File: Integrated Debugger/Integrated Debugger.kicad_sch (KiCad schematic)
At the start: 26 parts, among them J1 B2B GT-B0353FSV06-08B0201, J2 USB_C (PC <-> Host), U2 USBULC6-2M6

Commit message: feat: finish routing of components
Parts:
- removed D1: GREEN, symbol Picoballoon Passives:LED
- removed R4, R5, R6, R7: 100Ω, Picoballoon Passives:Resistor 0201, symbol Picoballoon Passives:Resistor
- removed TP1: SWDIO, symbol Connector:TestPoint_Small
- removed TP2: SWCLK, symbol Connector:TestPoint_Small
- removed TP3: NRST, symbol Connector:TestPoint_Small
- removed TP4: SWO, symbol Connector:TestPoint_Small
- removed TP5: D-, symbol Connector:TestPoint_Small
- removed TP6: D+, symbol Connector:TestPoint_Small
- added RN1: 100Ω, Picoballoon Passives:Resistor Pack YC248-JR-07100RL, symbol Picoballoon Passives:R_Pack08_Split
- D3, D4, D5: footprint (none) -> Picoballoon Passives:LED 0201
- R10, R8, R9: value 100Ω -> 1.5kΩ
- TP1: renamed from TP7; footprint (none) -> Picoballoon Mechanical & Misc:TestPoint
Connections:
- net MCU/LED0: now also R10.2; no longer D3.1 (K)
- net MCU/LED1: now also R9.2; no longer D4.1 (K)
- net MCU/LED2: now also R8.2; no longer D5.1 (K)
- net Target Frontend/xRST: now also RN1.16 (R1.2)
- net Target Frontend/xRXD: now also RN1.9 (R8.2)
- net Target Frontend/xTCK: now also RN1.13 (R4.2); no longer R10.1
- net Target Frontend/xTDI: now also RN1.15 (R2.2)
- net Target Frontend/xTDO: now also RN1.12 (R5.2); no longer R9.1
- net Target Frontend/xTMS: now also RN1.14 (R3.2)
- net Target Frontend/xTXD: now also RN1.11 (R6.2); no longer R8.1
- net Target/tRST: now also RN1.1 (R1.1)
- net Target/tRXD: now also RN1.8 (R8.1)
- net Target/tTCK: now also RN1.4 (R4.1); no longer R10.2
- net Target/tTDO: now also RN1.5 (R5.1); no longer R9.2
- net Target/tTMS: now also RN1.3 (R3.1)
- net Target/tTXD: now also RN1.6 (R6.1); no longer R8.2
- net at TP1.1: now also RN1.2 (R2.1)
- new net: D5.1 (K), R8.1
- new net: D3.1 (K), R10.1
- new net: D4.1 (K), R9.1
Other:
- sheet MCU: file mcu.kicad_sch -> MCU.kicad_sch
- sheet Power: file power.kicad_sch -> Power.kicad_sch
- sheet Power ports: added TARGET_EN; removed none
- sheet Target: file target.kicad_sch -> Target.kicad_sch
- sheet Target Frontend: file frontend.kicad_sch -> Frontend.kicad_sch
- sheet Target Frontend ports: added none; removed TARGET_EN

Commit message: feat: add manufacturing data
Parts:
- D2: JLCPCB Part # (none) -> C965555; LCSC Part # (none) -> C965555; MPN (none) -> WS2812B-2020
- D3: JLCPCB Part # (none) -> C3646923; LCSC Part # (none) -> C3646923; MPN (none) -> XL-0201SURC
- D4: JLCPCB Part # (none) -> C5440629; LCSC Part # (none) -> C5440629; MPN (none) -> XL-0201UOC
- D5: JLCPCB Part # (none) -> C5440628; LCSC Part # (none) -> C5440628; MPN (none) -> XL-0201UYC
- J2: JLCPCB Part # (none) -> C165948; LCSC Part # (none) -> C165948; MPN (none) -> TYPE-C-31-M-12
- R10, R11, R12, R8, R9: JLCPCB Part # (none) -> C155737; LCSC Part # (none) -> C155737; MPN (none) -> RC0201FR-071K5L
- R2, R3: JLCPCB Part # (none) -> C155743; LCSC Part # (none) -> C155743; MPN (none) -> RC0201FR-0722RL
- RN1: JLCPCB Part # (none) -> C695200; LCSC Part # (none) -> C695200; MPN (none) -> YC248-JR-07100RL
- TP1: now not fitted; now left out of the parts list
- U2: JLCPCB Part # (none) -> C2999115; LCSC Part # (none) -> C2999115; MPN (none) -> USBULC6-2M6

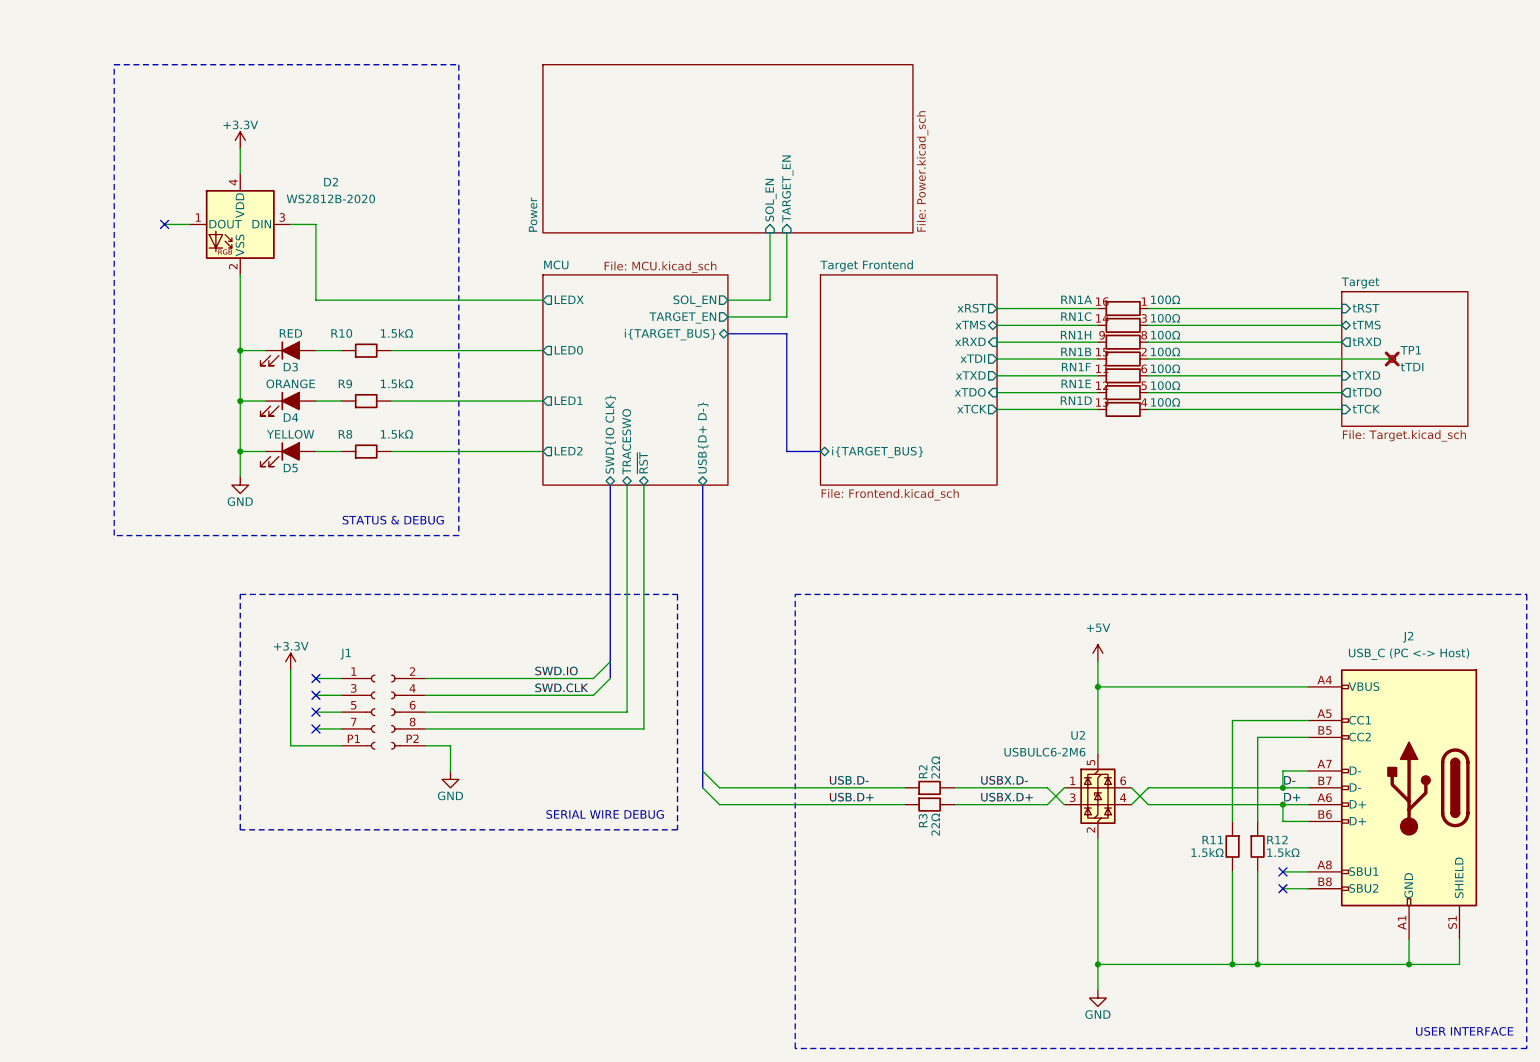
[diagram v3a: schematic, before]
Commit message: Schematic consistency improvements
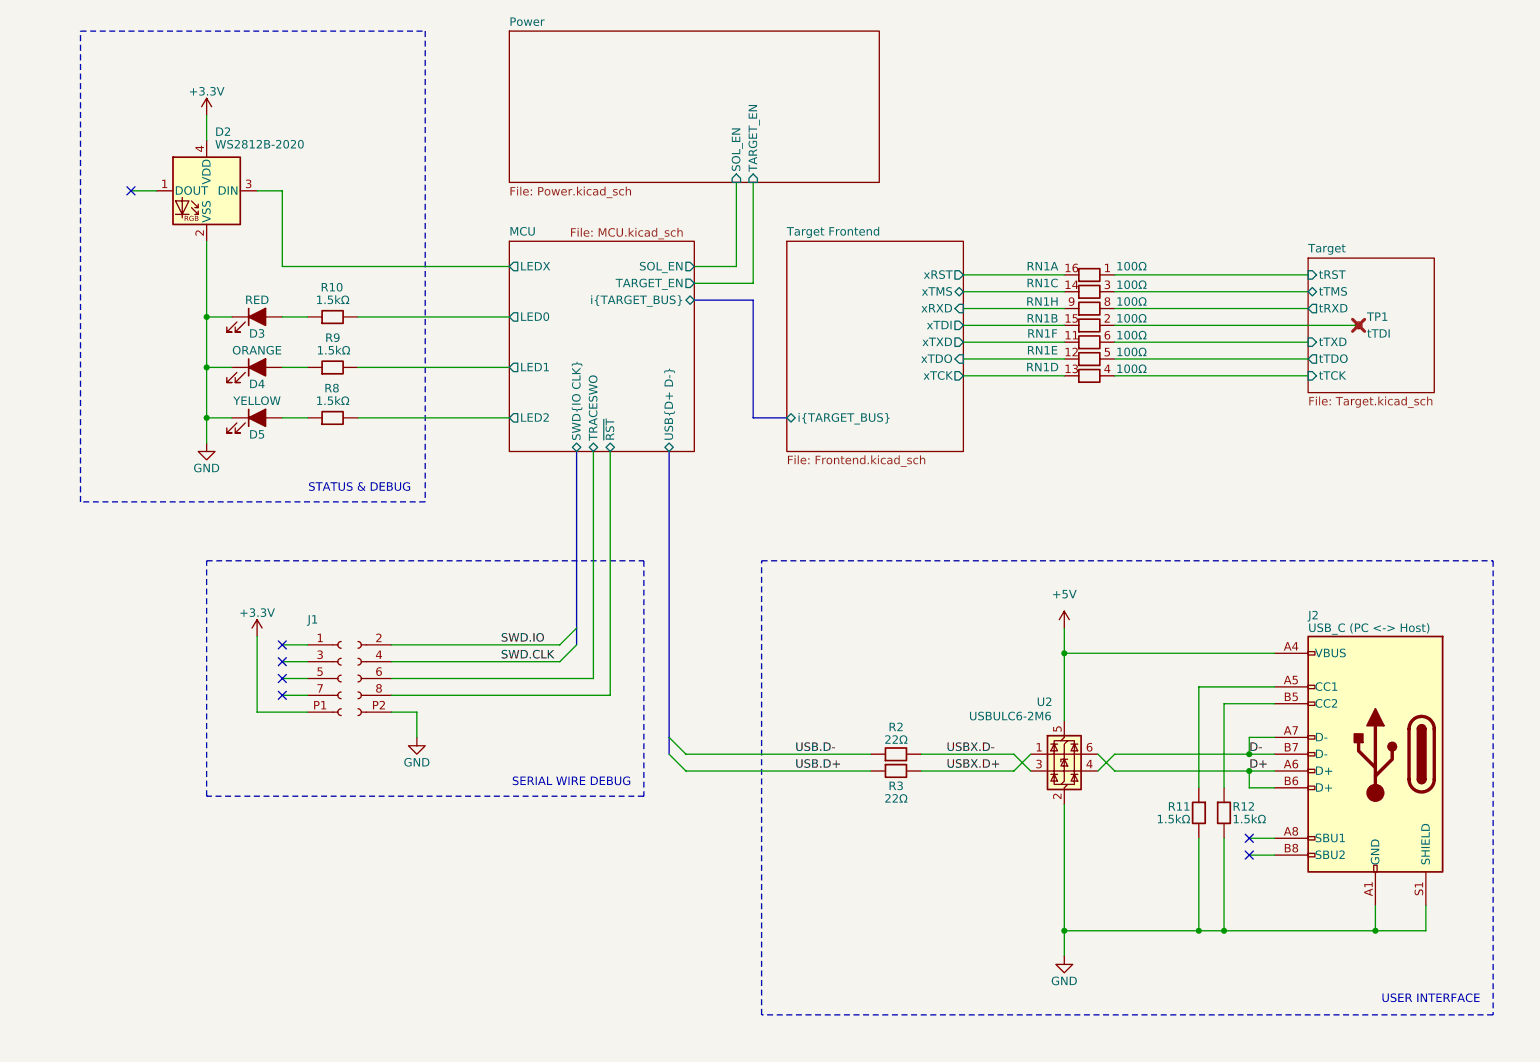
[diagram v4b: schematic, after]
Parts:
- RN1: symbol Picoballoon Passives:R_Pack08_Split -> Picoballoon Passives:Resistor array 8
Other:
- moved on the sheet: D2, D3, D4, D5, J1, J2, R10, R11, R12, R2, R3, R8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

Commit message: PCB improvements
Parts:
- removed RN1: 100Ω, Picoballoon Passives:Resistor Pack YC248-JR-07100RL, symbol Picoballoon Passives:Resistor array 8
- removed TP1: tTDI, Picoballoon Mechanical & Misc:TestPoint, symbol Connector:TestPoint_Small
- renumbered D2 to D1, D3 to D2, D4 to D3, D5 to D4, R10 to R1, R9 to R2, R8 to R3, R2 to R4, R3 to R5, R11 to R6, R12 to R7, U2 to U1
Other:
- removed sheet Target Frontend
- sheet Target ports: added i{TARGET_BUS}; removed tRST, tRXD, tTCK, tTDO, tTMS, tTXD

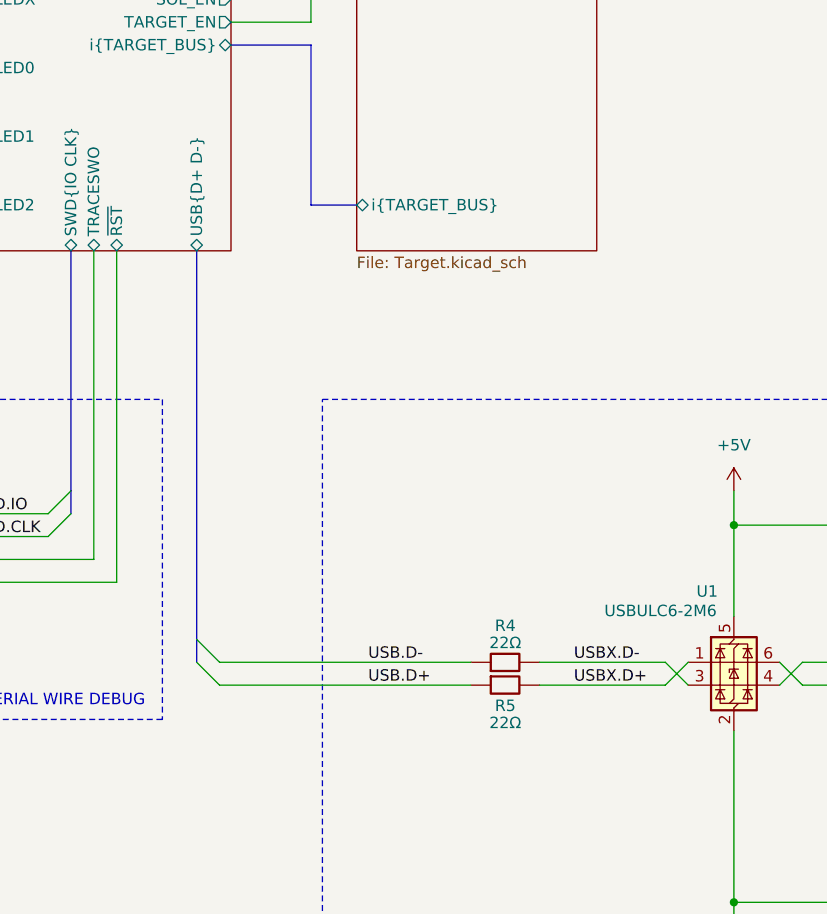
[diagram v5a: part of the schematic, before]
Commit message: feat: debugger flip swd connector, usb patch + stackup change
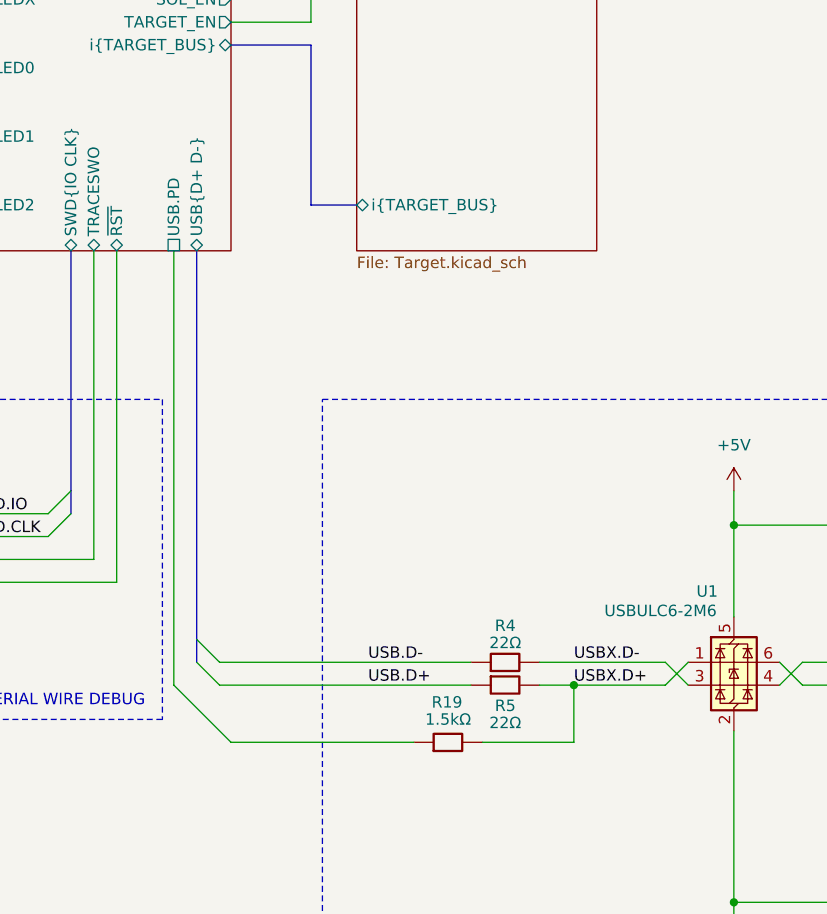
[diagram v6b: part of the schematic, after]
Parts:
- added R19: 1.5kΩ, Picoballoon Passives:Resistor 0201, symbol Picoballoon Passives:Resistor
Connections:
- net USBX.D+: now also R19.2
- new net MCU/USB.PD: R19.1
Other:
- sheet MCU ports: added USB.PD; removed none
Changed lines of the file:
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@@
+	)
+	(junction
+		(at 176.53 134.62)
+		(diameter 0)
+		(color 0 0 0 0)
 	)
 	(junction
@@
 	(wire
 		(pts
-			(xy 172.72 134.62) (xy 186.69 134.62)
+			(xy 172.72 134.62) (xy 176.53 134.62)
 		)
 		(stroke
@@
 	(wire
 		(pts
+			(xy 166.37 140.97) (xy 176.53 140.97)
+		)
+		(stroke
+			(width 0)
+			(type default)
+		)
+	)
+	(wire
+		(pts
 			(xy 248.92 154.94) (xy 248.92 158.75)
 		)
@@
 	(wire
 		(pts
+			(xy 132.08 134.62) (xy 138.43 140.97)
+		)
+		(stroke
+			(width 0)
+			(type default)
+		)
+	)
+	(wire
+		(pts
+			(xy 132.08 86.36) (xy 132.08 134.62)
+		)
+		(stroke
+			(width 0)
+			(type default)
+		)
+	)
+	(wire
+		(pts
 			(xy 194.31 116.84) (xy 226.06 116.84)
 		)
@@
 	(wire
 		(pts
+			(xy 176.53 134.62) (xy 176.53 140.97)
+		)
+		(stroke
+			(width 0)
+			(type default)
+		)
+	)
+	(wire
+		(pts
 			(xy 64.77 39.37) (xy 64.77 35.56)
 		)
@@
 		)
 	)
+	(wire
+		(pts
+			(xy 138.43 140.97) (xy 158.75 140.97)
+		)
+		(stroke
+			(width 0)
+			(type default)
+		)
+	)
 	(bus
 		(pts
@@
 		(pts
 			(xy 241.3 158.75) (xy 241.3 154.94)
+		)
+		(stroke
+			(width 0)
+			(type default)
+		)
+	)
+	(wire
+		(pts
+			(xy 176.53 134.62) (xy 186.69 134.62)
 		)
 		(stroke
@@
 		(pin "P2_2"
 		)
+		(pin "3"
+		)
+		(pin "P1"
+		)
+		(pin "7"
+		)
+		(pin "5"
+		)
+		(pin "1"
+		)
+		(pin "8"
+		)
+		(pin "6"
+		)
+		(pin "P1_2"
+		)
+		(pin "4"
+		)
+		(pin "2"
+		)
+		(pin "S4"
+		)
 		(pin "S3"
 		)
-		(pin "3"
-		)
-		(pin "P1"
-		)
-		(pin "7"
-		)
-		(pin "5"
-		)
-		(pin "1"
-		)
-		(pin "S4"
+		(pin "S1"
 		)
 		(pin "S2"
-		)
-		(pin "8"
-		)
-		(pin "6"
-		)
-		(pin "P1_2"
-		)
-		(pin "S1"
-		)
-		(pin "4"
-		)
-		(pin "2"
 		)
 		(instances
@@
 		)
 	)
+	(symbol
+		(lib_id "Picoballoon Passives:Resistor")
+		(at 162.56 140.97 90)
+		(unit 1)
+		(exclude_from_sim no)
+		(in_bom yes)
+		(on_board yes)
+		(dnp no)
+		(property "Reference" "R19"
+			(at 162.433 136.525 90)
+			(do_not_autoplace yes)
+			(effects
+				(font
+					(size 1.27 1.27)
+				)
+			)
+		)
+		(property "Value" "1.5kΩ"
+			(at 162.56 138.43 90)
+			(do_not_autoplace yes)
+			(effects
+				(font
+					(size 1.27 1.27)
+				)
+			)
+		)
+		(property "Footprint" "Picoballoon Passives:Resistor 0201"
+			(at 162.56 142.748 90)
+			(effects
+				(font
+					(size 1.27 1.27)
+				)
+				(hide yes)
+			)
+		)
+		(property "Datasheet" "~"
+			(at 162.56 140.97 0)
+			(effects
+				(font
+					(size 1.27 1.27)
+				)
+				(hide yes)
+			)
+		)
+		(property "Description" "Generic Resistor"
+			(at 162.56 140.97 0)
+			(effects
+				(font
+					(size 1.27 1.27)
+				)
+				(hide yes)
+			)
+		)
+		(property "MPN" "RC0201FR-071K5L"
+			(at 162.56 140.97 0)
+			(effects
+				(font
+					(size 1.27 1.27)
+				)
+				(hide yes)
+			)
+		)
+		(property "JLCPCB Part #" "C155737"
+			(at 162.56 140.97 90)
+			(effects
+				(font
+					(size 1.27 1.27)
+				)
+				(hide yes)
+			)
+		)
+		(property "LCSC Part #" "C155737"
+			(at 162.56 140.97 90)
+			(effects
+				(font
+					(size 1.27 1.27)
+				)
+				(hide yes)
+			)
+		)
+		(pin "2"
+		)
+		(pin "1"
+		)
+		(instances
+			(project "Integrated Debugger"
+				(path "/ce538ebe-fda9-4af3-9f8c-9fd5bf58f0e4"
+					(reference "R19")
+					(unit 1)
+				)
+			)
+		)
+	)
 	(sheet
 		(at 110.49 22.86)
@@
 			)
 		)
+		(pin "USB.PD" passive
+			(at 132.08 86.36 270)
+			(effects
+				(font
+					(size 1.27 1.27)
+				)
+				(justify left)
+			)
+		)

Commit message: Improve routing, placement & decorations, final check pass
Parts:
- J2: JLCPCB Part # C165948 -> C3197885; LCSC Part # C165948 -> C3197885; MPN TYPE-C-31-M-12 -> DX07S016JA1R1500
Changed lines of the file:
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@@
 			)
 		)
-		(property "JLCPCB Part #" "C165948"
+		(property "JLCPCB Part #" "C3197885"
 			(at 241.3 132.08 0)
 			(effects
@@
 			)
 		)
-		(property "LCSC Part #" "C165948"
+		(property "LCSC Part #" "C3197885"
 			(at 241.3 132.08 0)
 			(effects
@@
 			)
 		)
-		(property "MPN" "TYPE-C-31-M-12"
+		(property "MPN" "DX07S016JA1R1500"
 			(at 241.3 132.08 0)
 			(effects

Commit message: Update BOM
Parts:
- J1: symbol Picoballoon Mechanical & Misc:B2B GT-B0353FSV06-08B0201 -> Picoballoon Mechanical & Misc:B2B GT-B0353MSV04-08B0201; LCSC Part # C42385863 -> C42385857; MPN GT-B0353FSV06-08B0201 -> GT-B0353MSV04-08B0201
- renumbered R19 to R4, R4 to R5, R5 to R6, R6 to R7, R7 to R8
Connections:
- net +3.3V: no longer J1.S1, J1.S2
- net GND: no longer J1.S3, J1.S4
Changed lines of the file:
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@@
 		(on_board yes)
 		(dnp no)
-		(property "Reference" "R6"
+		(property "Reference" "R7"
 			(at 213.36 140.0175 0)
 			(do_not_autoplace yes)
@@
 			(project "Programmer"
 				(path "/ce538ebe-fda9-4af3-9f8c-9fd5bf58f0e4"
-					(reference "R6")
+					(reference "R7")
 					(unit 1)
 				)
@@
 		(on_board yes)
 		(dnp no)
-		(property "Reference" "R5"
+		(property "Reference" "R6"
 			(at 168.91 136.906 90)
 			(do_not_autoplace yes)
@@
 			(project "Programmer"
 				(path "/ce538ebe-fda9-4af3-9f8c-9fd5bf58f0e4"
-					(reference "R5")
+					(reference "R6")
 					(unit 1)
 				)
@@
 		(on_board yes)
 		(dnp no)
-		(property "Reference" "R4"
+		(property "Reference" "R5"
 			(at 168.91 128.016 90)
 			(do_not_autoplace yes)
@@
 			(project "Programmer"
 				(path "/ce538ebe-fda9-4af3-9f8c-9fd5bf58f0e4"
-					(reference "R4")
+					(reference "R5")
 					(unit 1)
 				)
@@
 		(dnp no)
 		(fields_autoplaced yes)
-		(property "Reference" "R7"
+		(property "Reference" "R8"
 			(at 219.71 140.0175 0)
 			(do_not_autoplace yes)
@@
 			(project ""
 				(path "/ce538ebe-fda9-4af3-9f8c-9fd5bf58f0e4"
-					(reference "R7")
+					(reference "R8")
 					(unit 1)
 				)
@@
 	)
 	(symbol
-		(lib_id "Picoballoon Mechanical & Misc:B2B GT-B0353FSV06-08B0201")
+		(lib_id "Picoballoon Mechanical & Misc:B2B GT-B0353MSV04-08B0201")
 		(at 86.36 120.65 0)
 		(unit 1)
@@
 			)
 		)
-		(property "Datasheet" "https://www.lcsc.com/datasheet/lcsc_datasheet_2411191029_G-Switch-GT-B0353FSV06-10B0201_C42385864.pdf"
+		(property "Datasheet" "https://www.lcsc.com/datasheet/C42385857.pdf"
 			(at 86.36 151.13 0)
 			(effects
@@
 			)
 		)
-		(property "MPN" "GT-B0353FSV06-08B0201"
+		(property "MPN" "GT-B0353MSV04-08B0201"
 			(at 86.36 153.67 0)
 			(effects
@@
 			)
 		)
-		(property "LCSC Part #" "C42385863"
+		(property "LCSC Part #" "C42385857"
 			(at 86.36 153.67 0)
 			(effects
@@
 		)
 		(pin "2"
-		)
-		(pin "S4"
-		)
-		(pin "S3"
-		)
-		(pin "S1"
-		)
-		(pin "S2"
 		)
 		(instances
@@
 		(on_board yes)
 		(dnp no)
-		(property "Reference" "R19"
+		(property "Reference" "R4"
 			(at 162.433 136.525 90)
 			(do_not_autoplace yes)
@@
 			(project "Integrated Debugger"
 				(path "/ce538ebe-fda9-4af3-9f8c-9fd5bf58f0e4"
-					(reference "R19")
-					(unit 1)
-				)
+					(reference "R4")
+					(unit 1)
+				)
